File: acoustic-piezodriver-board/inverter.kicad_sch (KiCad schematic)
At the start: 29 parts, among them P201 WJ128V-5.0-3P, U201 UCC27282DR, U202 UCC27282DR, U6 NCE6005AS, U7 NCE6005AS

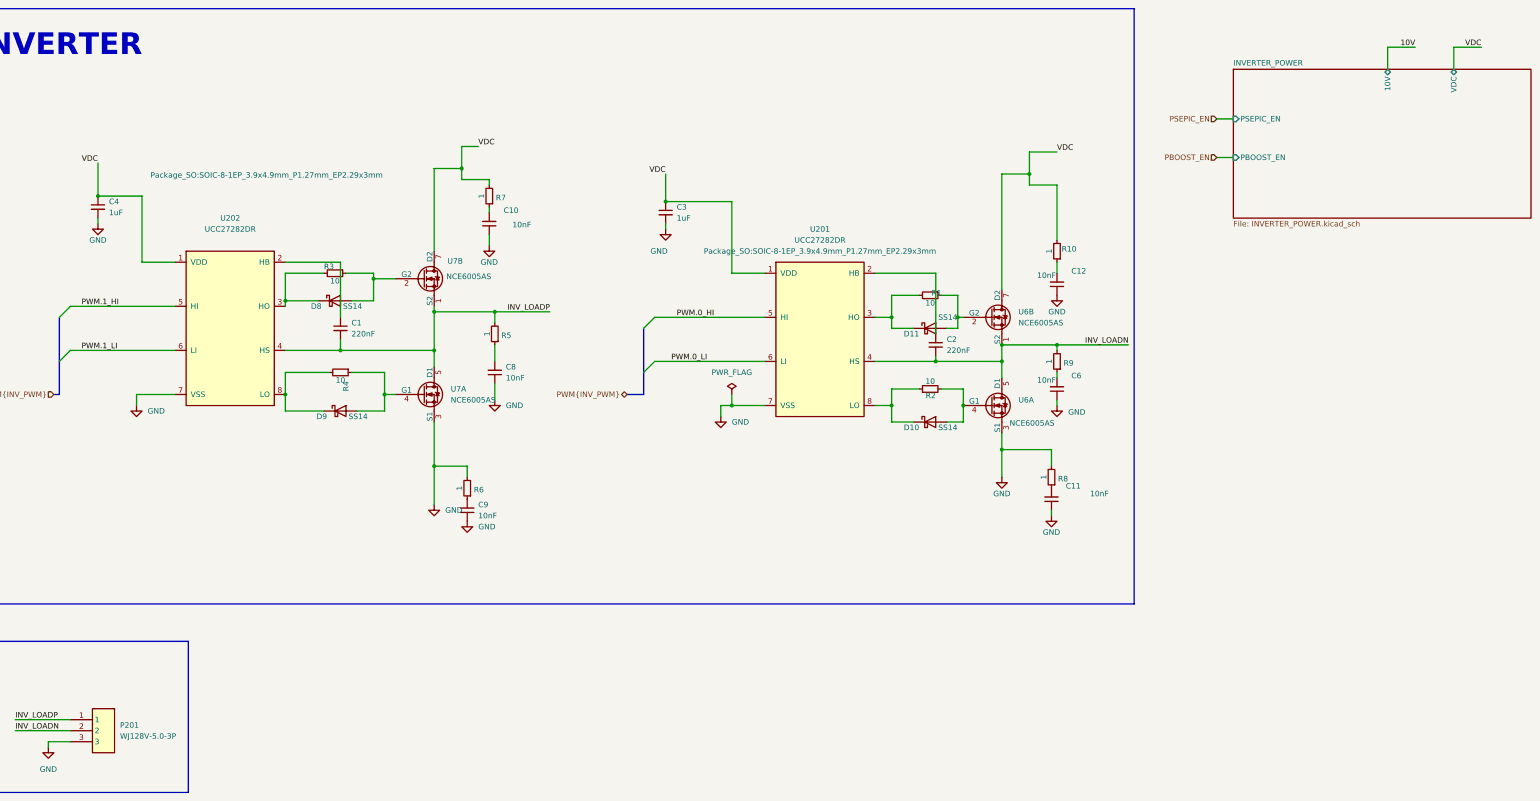
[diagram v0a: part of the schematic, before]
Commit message: [schematic] added adc for temperature measurement, current sense resistors, [layout] component placement, connector placement
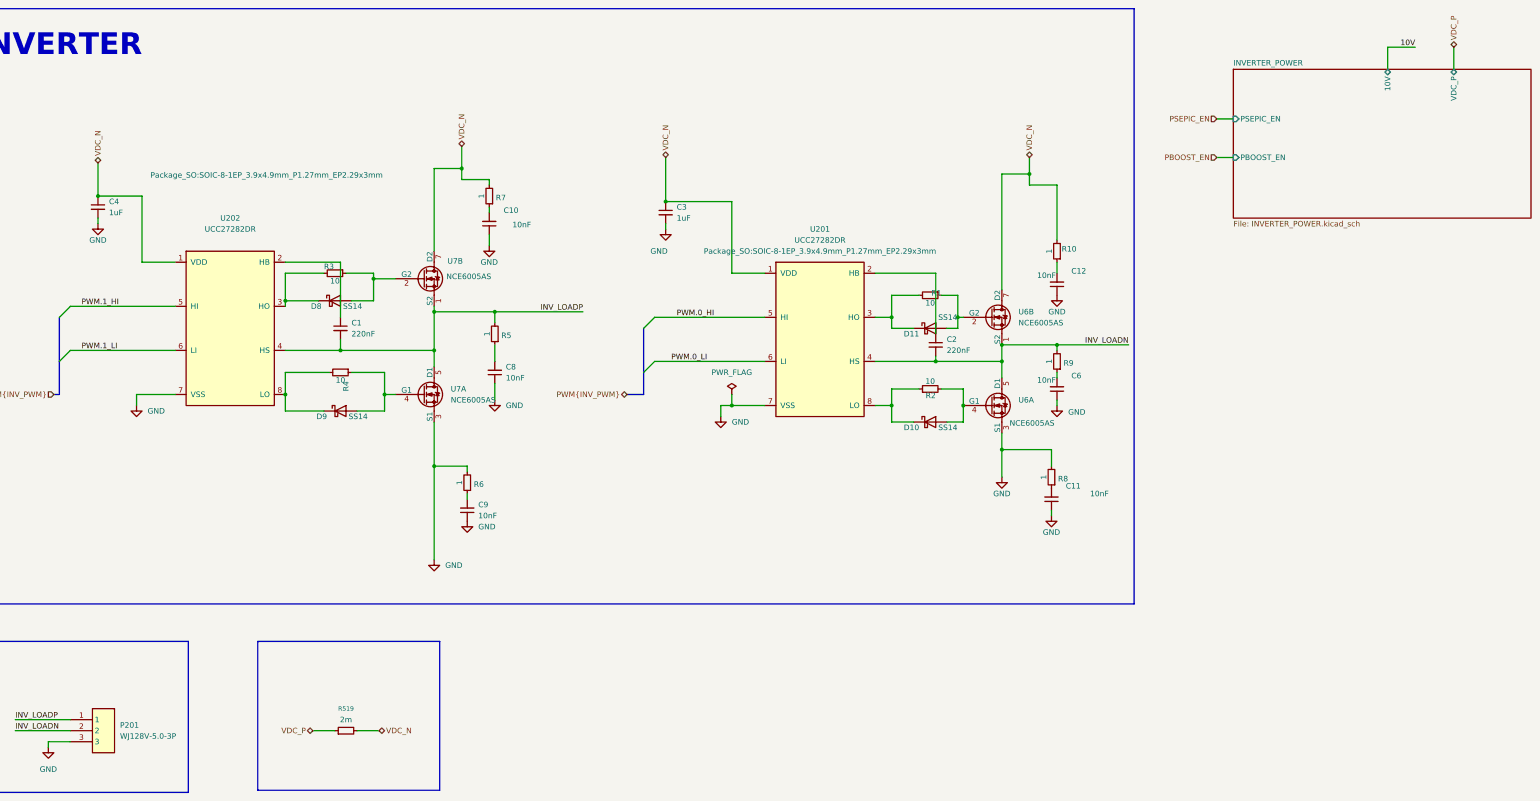
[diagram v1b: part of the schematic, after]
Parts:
- added R519: 2m, Resistor_SMD:R_2512_6332Metric, symbol Device:R_Small
- U7: footprint (none) -> Package_SO:SOIC-8_3.9x4.9mm_P1.27mm
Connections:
- net VDC renamed VDC_N
- net VDC_N: now also R519.2
- new net VDC_P: R519.1
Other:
- sheet INVERTER_POWER ports: added VDC_P; removed VDC
- moved on the sheet: R6

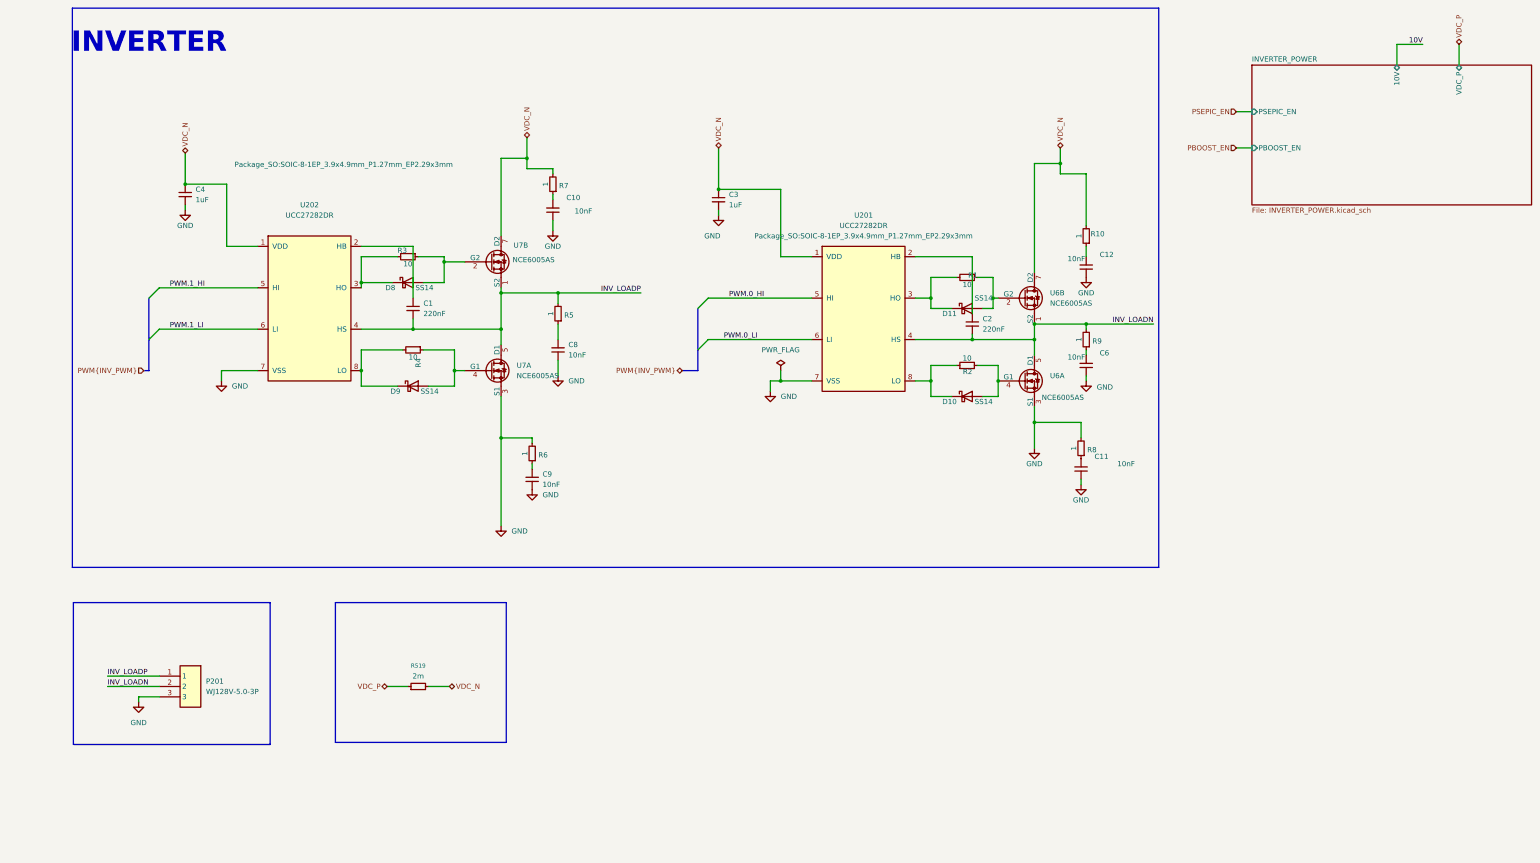
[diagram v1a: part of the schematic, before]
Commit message: found hal-sensor, replaced with different one for lower voltage signal source impedance, reorganised schematic
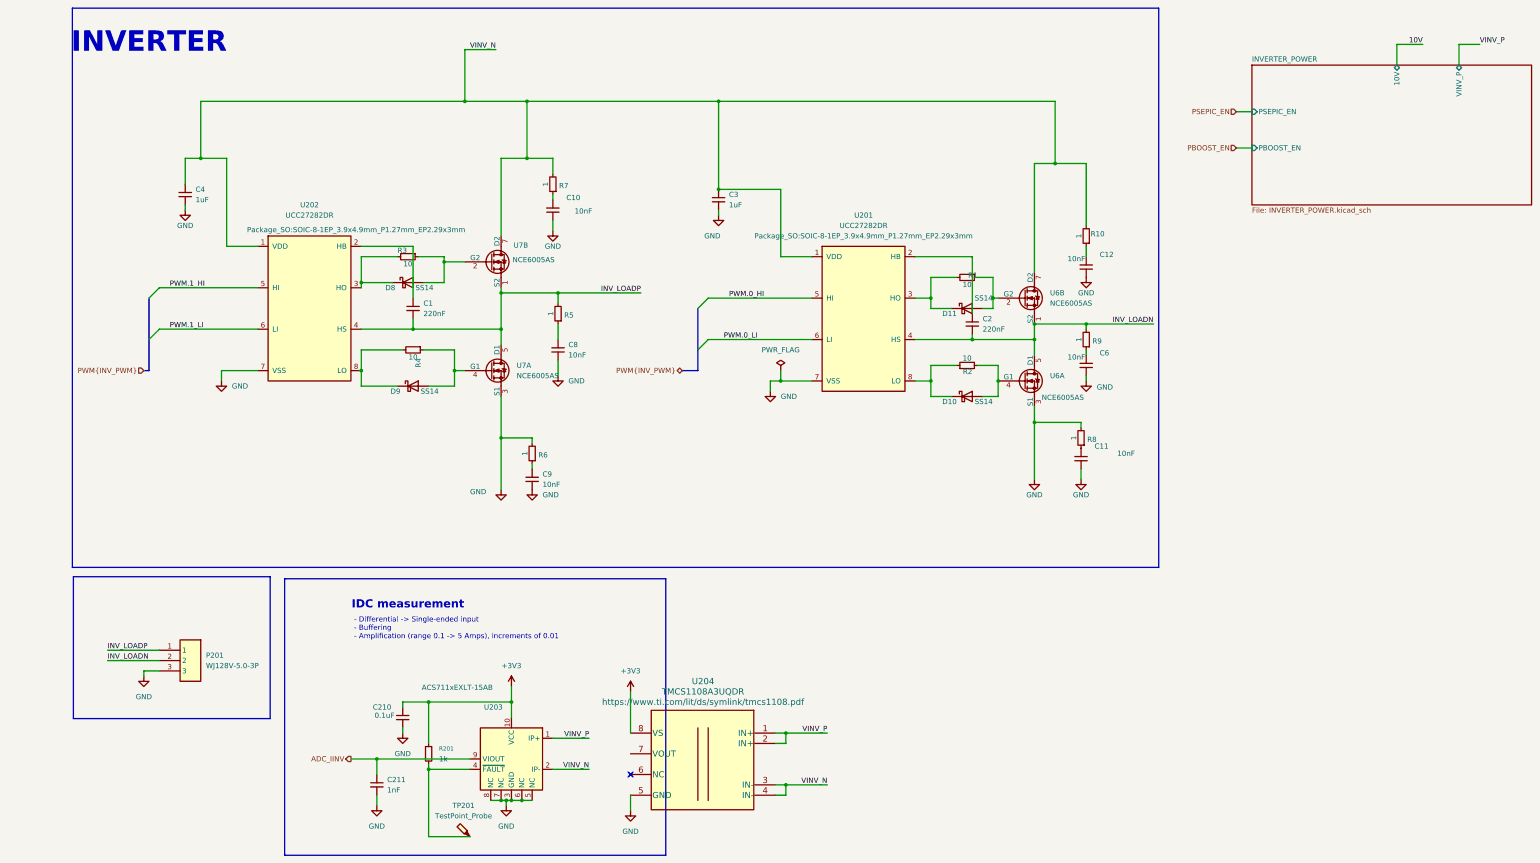
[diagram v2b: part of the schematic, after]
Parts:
- removed R519: 2m, Resistor_SMD:R_2512_6332Metric, symbol Device:R_Small
- added C210: 0.1uF, Capacitor_SMD:C_0402_1005Metric, symbol Device:C_Small
- added C211: 1nF, Capacitor_SMD:C_0402_1005Metric, symbol Device:C_Small
- added R201: 1k, Resistor_SMD:R_0603_1608Metric, symbol Device:R_Small
- added TP201: TestPoint_Probe, TestPoint:TestPoint_Pad_D1.0mm, symbol Connector:TestPoint_Probe
- added U203: ACS711xEXLT-15AB, Sensor_Current:Allegro_QFN-12-10-1EP_3x3mm_P0.5mm, symbol Sensor_Current:ACS711xEXLT-15AB
- added U204: TMCS1108A3UQDR, iw-power:TMCS1108A3UQDR, symbol iw-power:TMCS1108A3UQDR
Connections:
- net GND: now also C210.2, C211.2, U203.3 (GND), U203.5 (NC), U203.6 (NC), U203.7 (NC), U203.8 (NC), U204.5 (GND)
- net VDC_N renamed VINV_N
- net VINV_N: now also U203.2 (IP-), U204.3 (IN-), U204.4 (IN-)
- new net: R201.2, TP201.1, U203.4 (~{FAULT})
- new net +3V3: C210.1, R201.1, U203.10 (VCC), U204.8 (VS)
- new net ADC_IINV: C211.1, U203.9 (VIOUT)
- new net VINV_P: U203.1 (IP+), U204.1 (IN+), U204.2 (IN+)
- no-connect marks 0 -> 1
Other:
- sheet INVERTER_POWER ports: added VINV_P; removed VDC_P
- note added: "- Differential -> Single-ended input - Buffering - Amplification (range 0.1 -> 5 Amps), increments of 0.01"
- note added: "IDC measurement"
- moved on the sheet: C11, P201, R8

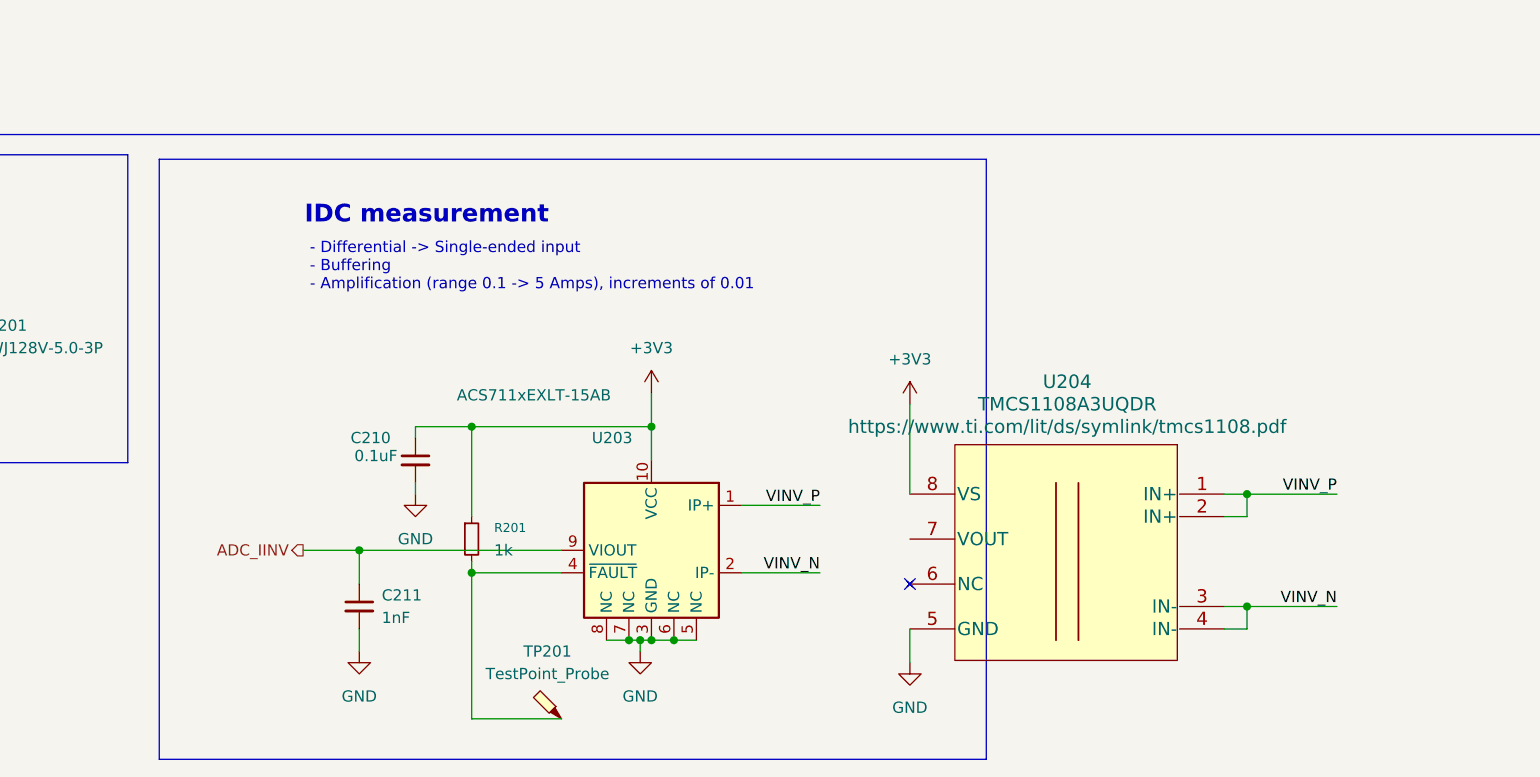
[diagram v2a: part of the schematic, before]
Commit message: added new notes + schematic component hal sensors
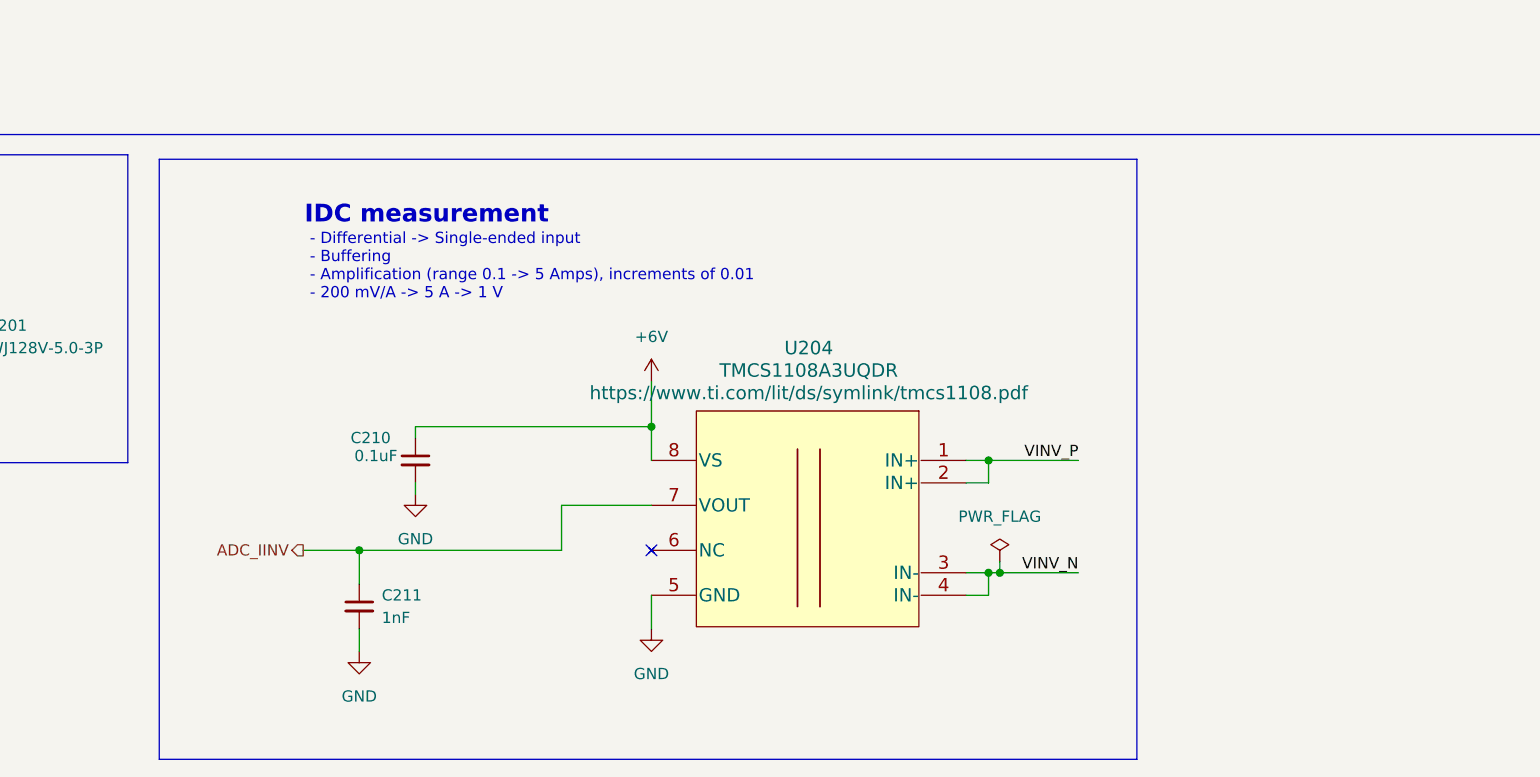
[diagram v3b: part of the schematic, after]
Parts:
- removed R201: 1k, Resistor_SMD:R_0603_1608Metric, symbol Device:R_Small
- removed TP201: TestPoint_Probe, TestPoint:TestPoint_Pad_D1.0mm, symbol Connector:TestPoint_Probe
- removed U203: ACS711xEXLT-15AB, Sensor_Current:Allegro_QFN-12-10-1EP_3x3mm_P0.5mm, symbol Sensor_Current:ACS711xEXLT-15AB
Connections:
- net ADC_IINV: now also U204.7 (VOUT)
- net +3V3 renamed +6V
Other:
- note added: "- Differential -> Single-ended input - Buffering - Amplification (range 0.1 -> 5 Amps), increments of 0.01 - 200 mV/A -> 5 A -> 1 V"
- note removed: "- Differential -> Single-ended input - Buffering - Amplification (range 0.1 -> 5 Amps), increments of 0.01"
- moved on the sheet: U204
